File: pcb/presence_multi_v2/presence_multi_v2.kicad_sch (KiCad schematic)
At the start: 27 parts, among them J1 USB_C_Receptacle_USB2.0_16P, J2 TC2050, J3 Conn_01x06_Socket, U2 AMS1117-3.3, U3 CH340E, Y1 Wurth 830050789

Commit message: started actual PCB design
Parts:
- PS1, PS2: footprint Connector_JST:JST_XH_B5B-XH-A_1x05_P2.50mm_Vertical -> Connector_JST:JST_PH_B5B-PH-K_1x05_P2.00mm_Vertical
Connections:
- net I2C20_SCL: now also MCU1.22 (P1.05/AIN1); no longer MCU1.20 (P1.07/AIN3)
- net I_AIR1: now also MCU1.20 (P1.07/AIN3); no longer MCU1.22 (P1.05/AIN1)
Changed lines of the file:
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@@
 	(wire
 		(pts
-			(xy 223.52 83.82) (xy 231.14 83.82)
+			(xy 223.52 83.82) (xy 229.87 83.82)
 		)
 		(stroke
@@
 	(wire
 		(pts
+			(xy 229.87 92.71) (xy 231.14 92.71)
+		)
+		(stroke
+			(width 0)
+			(type default)
+		)
+	)
+	(wire
+		(pts
 			(xy 186.69 161.29) (xy 195.58 161.29)
 		)
@@
 	(wire
 		(pts
-			(xy 231.14 83.82) (xy 231.14 95.25)
+			(xy 229.87 83.82) (xy 229.87 92.71)
 		)
 		(stroke
@@
 	(wire
 		(pts
-			(xy 231.14 82.55) (xy 236.22 82.55)
+			(xy 226.06 88.9) (xy 231.14 88.9)
 		)
 		(stroke
@@
 	(wire
 		(pts
-			(xy 133.35 91.44) (xy 130.81 91.44)
+			(xy 236.22 90.17) (xy 236.22 95.25)
 		)
 		(stroke
@@
 	(wire
 		(pts
-			(xy 290.83 120.65) (xy 304.8 120.65)
+			(xy 133.35 91.44) (xy 130.81 91.44)
 		)
 		(stroke
@@
 	(wire
 		(pts
-			(xy 111.76 62.23) (xy 111.76 64.77)
+			(xy 290.83 120.65) (xy 304.8 120.65)
 		)
 		(stroke
@@
 	(wire
 		(pts
-			(xy 226.06 85.09) (xy 226.06 95.25)
+			(xy 111.76 62.23) (xy 111.76 64.77)
 		)
 		(stroke
@@
 	(wire
 		(pts
-			(xy 220.98 85.09) (xy 226.06 85.09)
+			(xy 220.98 90.17) (xy 236.22 90.17)
 		)
 		(stroke
@@
 	(wire
 		(pts
-			(xy 220.98 77.47) (xy 220.98 85.09)
+			(xy 220.98 77.47) (xy 220.98 90.17)
+		)
+		(stroke
+			(width 0)
+			(type default)
+		)
+	)
+	(wire
+		(pts
+			(xy 231.14 92.71) (xy 231.14 95.25)
 		)
 		(stroke
@@
 	(wire
 		(pts
-			(xy 231.14 77.47) (xy 231.14 82.55)
+			(xy 231.14 77.47) (xy 231.14 88.9)
 		)
 		(stroke
@@
 	(wire
 		(pts
+			(xy 226.06 88.9) (xy 226.06 95.25)
+		)
+		(stroke
+			(width 0)
+			(type default)
+		)
+	)
+	(wire
+		(pts
 			(xy 87.63 62.23) (xy 87.63 81.28)
 		)
@@
 	(wire
 		(pts
-			(xy 236.22 82.55) (xy 236.22 95.25)
-		)
-		(stroke
-			(width 0)
-			(type default)
-		)
-	)
-	(wire
-		(pts
 			(xy 288.29 167.64) (xy 304.8 167.64)
 		)
@@
 	)
 	(label "I2C20_SDA"
-		(at 231.14 95.25 90)
+		(at 228.6 83.82 180)
 		(effects
 			(font
 				(size 1.27 1.27)
 			)
-			(justify left bottom)
+			(justify right bottom)
 		)
 	)
@@
 	)
 	(label "I_AIR1"
-		(at 236.22 93.98 90)
+		(at 231.14 81.28 0)
 		(effects
 			(font
@@
 	)
 	(label "I2C20_SCL"
-		(at 226.06 95.25 90)
+		(at 220.98 88.9 180)
 		(effects
 			(font
 				(size 1.27 1.27)
 			)
-			(justify left bottom)
+			(justify right bottom)
 		)
 	)
@@
 			)
 		)
-		(property "Footprint" "Connector_JST:JST_XH_B5B-XH-A_1x05_P2.50mm_Vertical"
+		(property "Footprint" "Connector_JST:JST_PH_B5B-PH-K_1x05_P2.00mm_Vertical"
 			(at 309.88 115.57 0)
 			(effects
@@
 			)
 		)
-		(property "Footprint" "Connector_JST:JST_XH_B5B-XH-A_1x05_P2.50mm_Vertical"
+		(property "Footprint" "Connector_JST:JST_PH_B5B-PH-K_1x05_P2.00mm_Vertical"
 			(at 309.88 138.43 0)
 			(effects

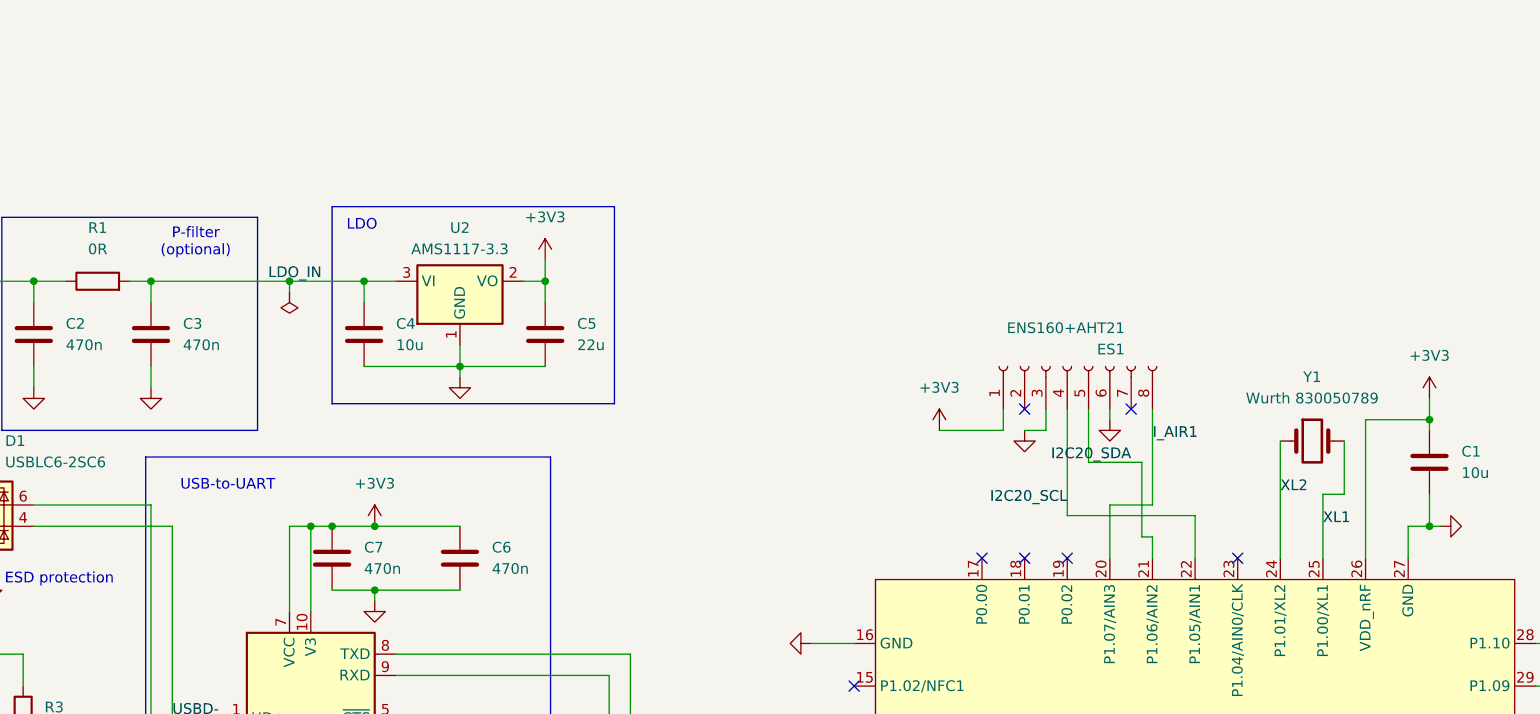
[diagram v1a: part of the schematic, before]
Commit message: replaced ASM1117 with LDL1117, removed 8 pin socket, added 3 4-pin JST-PH connectors
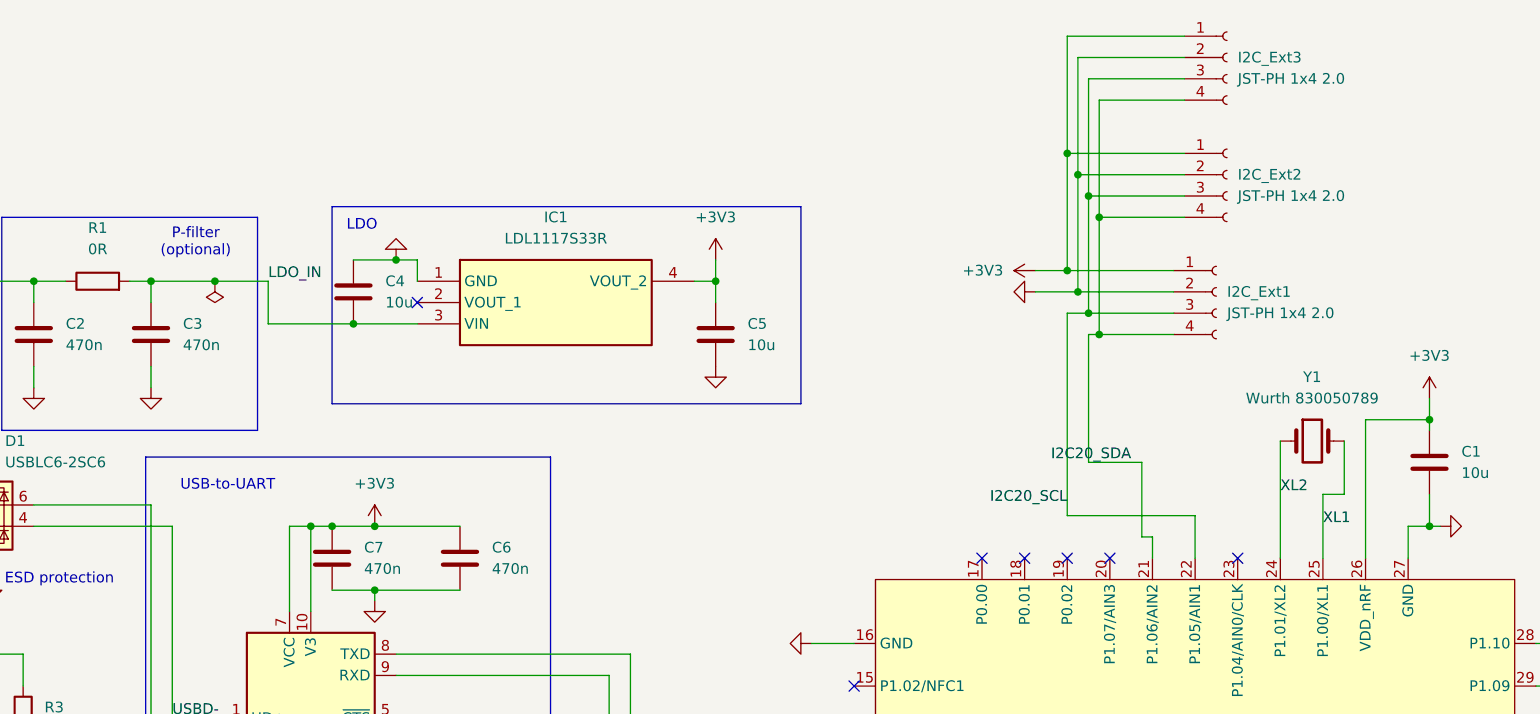
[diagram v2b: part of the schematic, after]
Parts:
- removed ES1: ENS160+AHT21, Connector_PinSocket_2.54mm:PinSocket_1x08_P2.54mm_Vertical, symbol Connector:Conn_01x08_Socket
- removed U2: AMS1117-3.3, Package_TO_SOT_SMD:SOT-223-3_TabPin2, symbol Regulator_Linear:AMS1117-3.3
- added I2C_Ext1, I2C_Ext2, I2C_Ext3: JST-PH 1x4 2.0, Connector_JST:JST_PH_B4B-PH-K_1x04_P2.00mm_Vertical, symbol Connector:Conn_01x04_Socket
- added IC1: LDL1117S33R, theorlangur:LDL1117S33R, symbol theorlangur:LDL1117S33R
- C5: value 22u -> 10u
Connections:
- net +3V3: now also I2C_Ext1.1 (Pin_1), I2C_Ext2.1 (Pin_1), I2C_Ext3.1 (Pin_1), IC1.4 (VOUT_2)
- net GND: now also C4.1, I2C_Ext1.2 (Pin_2), I2C_Ext2.2 (Pin_2), I2C_Ext3.2 (Pin_2), IC1.1 (GND); no longer C4.2
- net I2C20_SCL: now also I2C_Ext1.3 (Pin_3), I2C_Ext2.3 (Pin_3), I2C_Ext3.3 (Pin_3)
- net I2C20_SDA: now also I2C_Ext1.4 (Pin_4), I2C_Ext2.4 (Pin_4), I2C_Ext3.4 (Pin_4)
- net LDO_IN: now also C4.2, IC1.3 (VIN); no longer C4.1
- net I_AIR1: no longer names the net of MCU1.20 (P1.07/AIN3)
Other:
- moved on the sheet: C4, C5

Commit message: added buttons, configured PCB settings
removed layers
configured pre-defined ruls (constraints)
added default sizes
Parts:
- added BTN1: nRST, Button_Switch_SMD:SW_SPST_TS-1088-xR020, symbol Switch:SW_Push
- added BTN2: MCUBoot, Button_Switch_SMD:SW_SPST_TS-1088-xR020, symbol Switch:SW_Push
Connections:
- net GND: now also BTN1.1, BTN2.1
- net USBD+: now also D1.4 (I/O2), U3.1 (UD+); no longer D1.6 (I/O1), U3.2 (UD-)
- net USBD-: now also D1.6 (I/O1), U3.2 (UD-); no longer D1.4 (I/O2), U3.1 (UD+)
- net nRST: now also BTN1.2
- net BTN_MCUBoot: now reaches MCU1.17 (P0.00)
- net BTN_MCUBoot: now also BTN2.2
- no-connect marks 20 -> 22
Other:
- note added: "Buttons"
